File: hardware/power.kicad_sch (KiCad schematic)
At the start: 64 parts, among them IC1 TPS54202HDDCR, Q1 SI2347DS-T1-GE3, Q2 LMR51635XDDCR, Q3 LMR51635XDDCR, T1 TP_VCC, T10 TP_+5V, T11 TP_+5V, T2 TP_VCC, T3 TP_VCC, T4 TP_+6V6S1, T5 TP_+6V6S1, T6 TP_+6V6S2, T7 TP_+6V6S2, T8 TP_VCC, T9 TP_+3V3, U2 LM1117-3.3

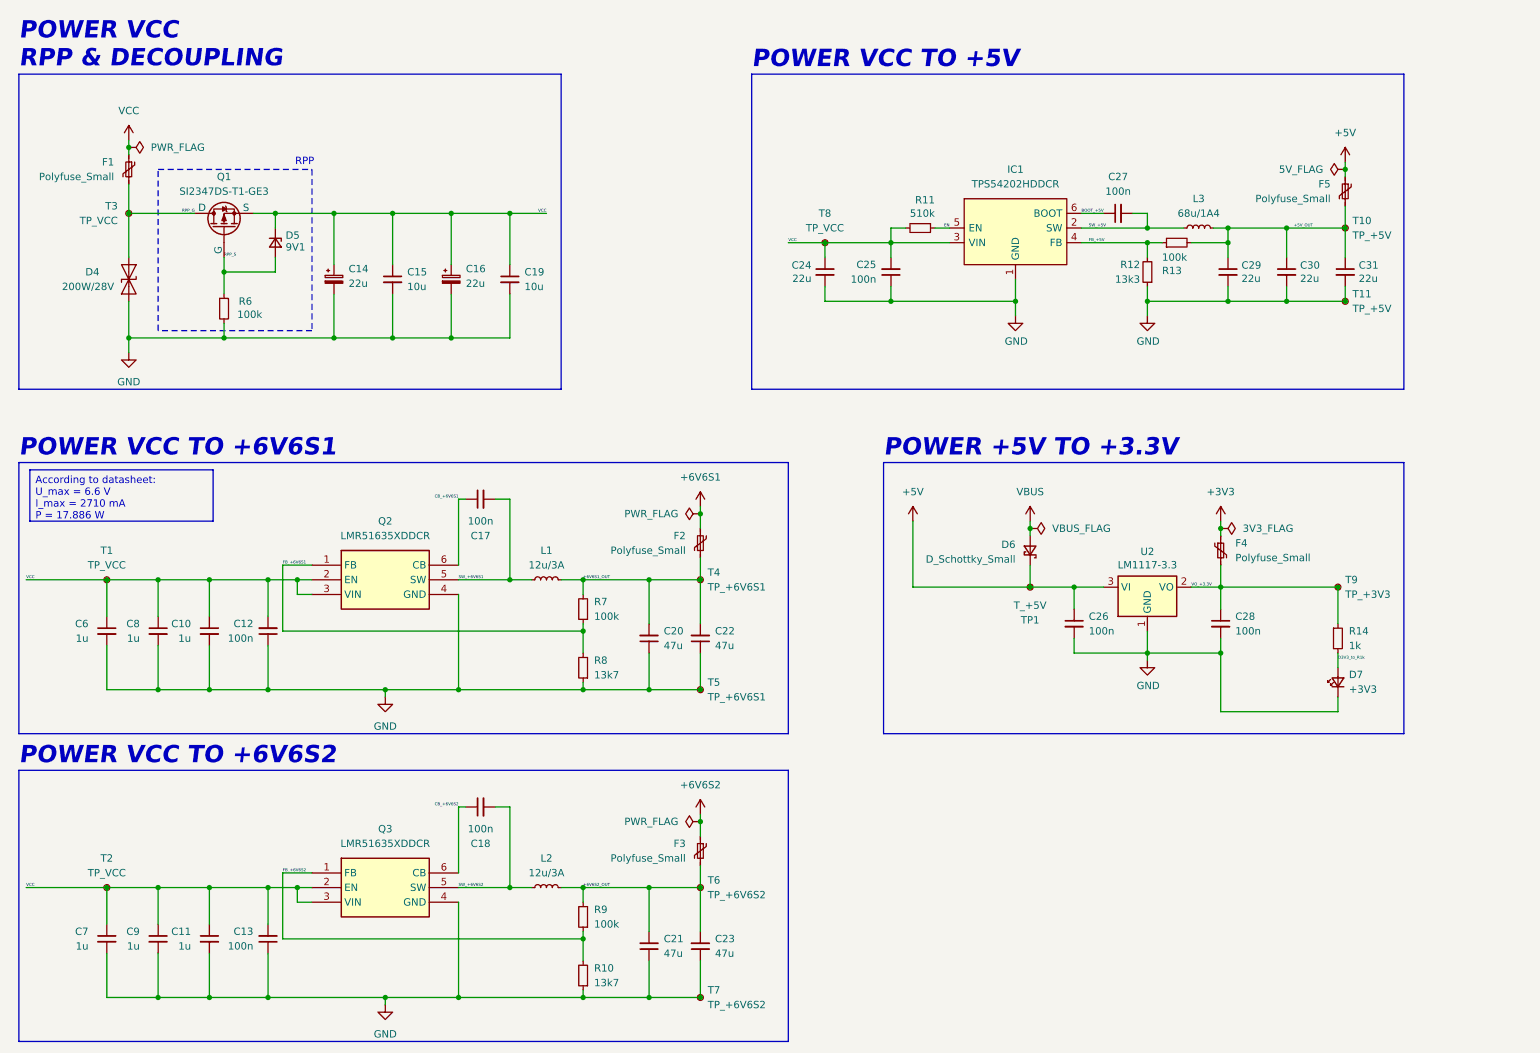
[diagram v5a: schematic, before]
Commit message: VCC to RPP & RPP to rest routing
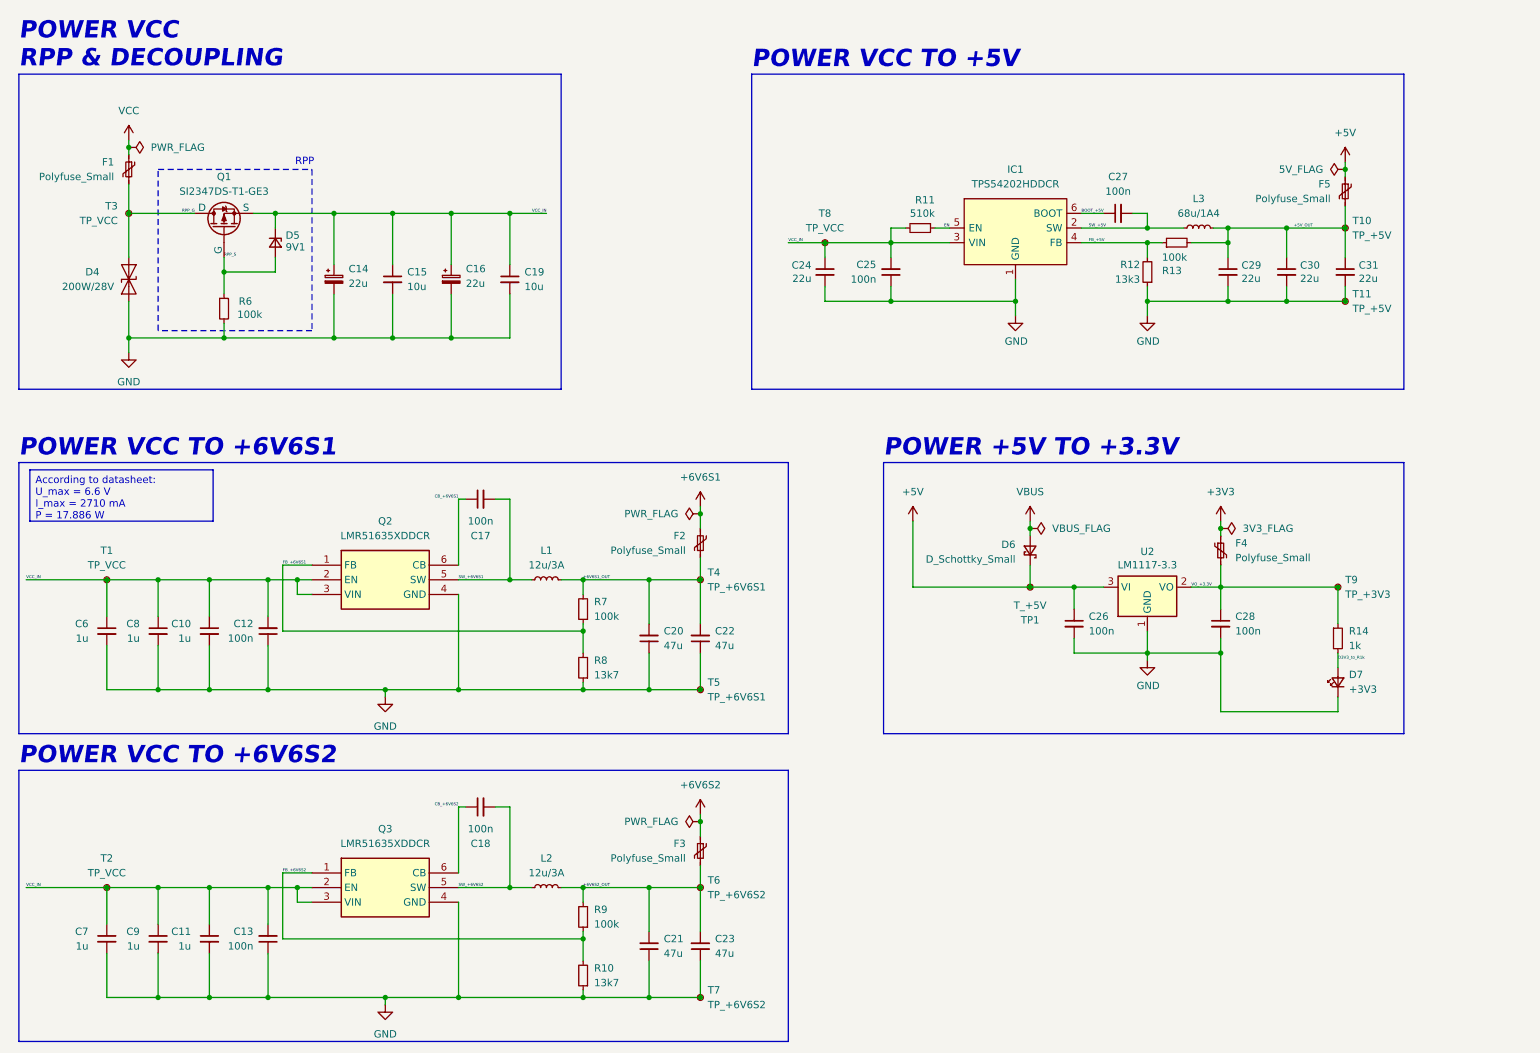
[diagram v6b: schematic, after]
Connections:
- net VCC: no longer C10.1, C11.1, C12.2, C13.2, C14.1, C15.1, C16.1, C19.1, C24.1, C25.2, C6.1, C7.1, C8.1, C9.1, D5.1 (K), IC1.3 (VIN), Q1.3 (S), Q2.2 (EN), Q2.3 (VIN), Q3.2 (EN), Q3.3 (VIN), R11.2, T1.1, T2.1, T8.1
- new net VCC_IN: C10.1, C11.1, C12.2, C13.2, C14.1, C15.1, C16.1, C19.1, C24.1, C25.2, C6.1, C7.1, C8.1, C9.1, D5.1 (K), IC1.3 (VIN), Q1.3 (S), Q2.2 (EN), Q2.3 (VIN), Q3.2 (EN), Q3.3 (VIN), R11.2, T1.1, T2.1, T8.1
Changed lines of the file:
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@@
 		)
 	)
-	(label "VCC"
+	(label "VCC_IN"
 		(at 107.95 50.8 180)
 		(effects
@@
 		)
 	)
-	(label "VCC"
+	(label "VCC_IN"
 		(at 17.78 114.3 0)
 		(effects
@@
 		)
 	)
-	(label "VCC"
+	(label "VCC_IN"
 		(at 17.78 167.64 0)
 		(effects
@@
 		)
 	)
-	(label "VCC"
+	(label "VCC_IN"
 		(at 149.86 55.88 0)
 		(effects

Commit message: Update
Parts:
- removed Q1: SI2347DS-T1-GE3, Package_TO_SOT_SMD:SOT-23-3, symbol Simulation_SPICE:PMOS
- added C34, C35, C37: 22u, Capacitor_SMD:C_0805_2012Metric_Pad1.18x1.45mm_HandSolder, symbol Device:C_Small
- added C36: 10u, Capacitor_SMD:C_0603_1608Metric_Pad1.08x0.95mm_HandSolder, symbol Device:C_Small
- added Q1: SI2347DS-T1-GE3, Package_TO_SOT_SMD:SOT-23-3, symbol Transistor_FET:Q_PMOS_GSD
- D6: value D_Schottky_Small -> SKL34
- F1: value Polyfuse_Small -> MFU0805FF00500P500
- F2, F3: value Polyfuse_Small -> 0805L400SLWR
- F4, F5: value Polyfuse_Small -> PICOSMDC050S-2
- L1, L2: value 12u/3A -> 12u/4A; footprint Inductor_SMD:L_TDK_VLS6045EX_VLS6045AF -> Inductor_SMD:L_Bourns_SRN6045TA; Mouser Price/Stock https://www.mouser.pl/ProductDetail/TDK/VLS6045EX-150M?qs=o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 -> https://www.mouser.pl/ProductDetail/Bourns/SRN6045TA-120M?q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
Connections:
- net RPP_S is gone; now on net RPP_G: D5.2 (A), R6.1
- net +5V: now also C36.1
- net GND: now also C34.1, C35.1, C36.2, C37.2
- net RPP_G: now also Q1.1 (G); no longer D4.2 (A2), F1.2, T3.1
- net VCC_IN: now also C34.2, C35.2, Q1.2 (S)
- net VO_+3.3V: now also C37.1
- new net RPP_D: D4.2 (A2), F1.2, Q1.3 (D), T3.1
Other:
- note added: "POWER VCC TO +6V6 SERVO1"
- note added: "POWER VCC TO +6V6 SERVO2"
- note removed: "POWER VCC TO +6V6S1"
- note removed: "POWER VCC TO +6V6S2"
- moved on the sheet: C10, C11, C12, C13, C14, C15, C16, C17, C18, C19, C20, C21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

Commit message: pcb update
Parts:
- TP1: value T_+5V -> TP_+5V
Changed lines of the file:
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@@
 			)
 		)
-		(property "Value" "T_+5V"
+		(property "Value" "TP_+5V"
 			(at 179.07 118.745 90)
 			(effects
